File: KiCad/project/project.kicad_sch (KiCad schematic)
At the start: 8 parts, among them U1 NUCLEO-L476RG

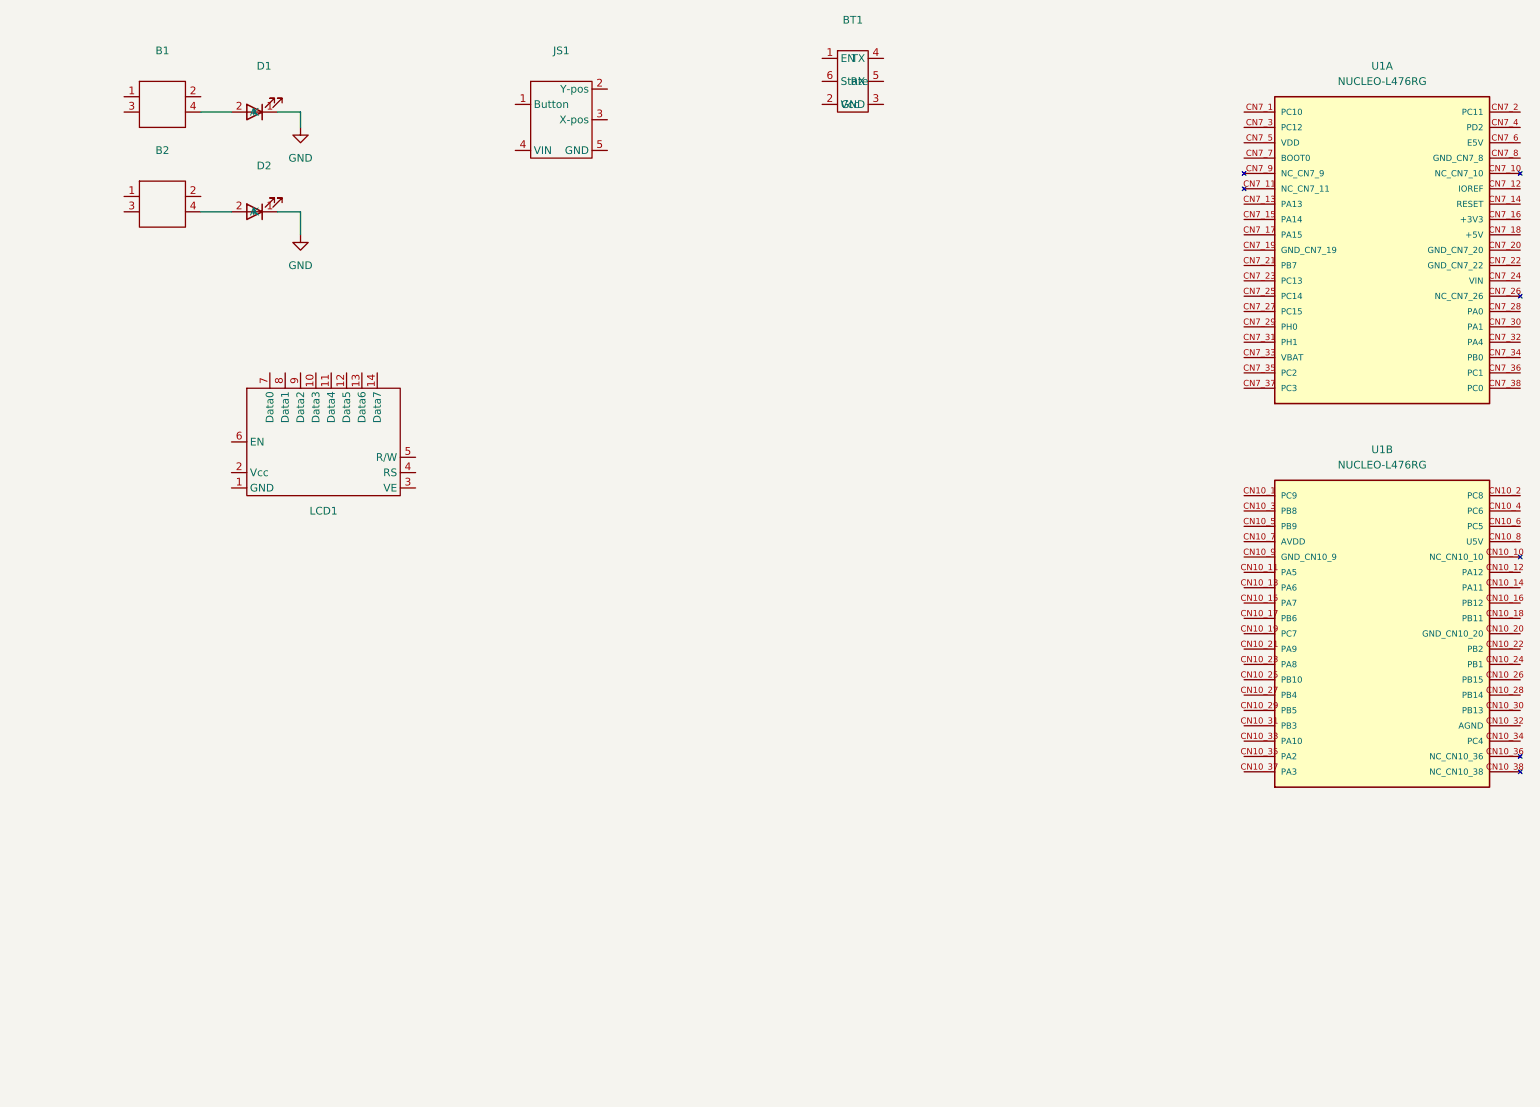
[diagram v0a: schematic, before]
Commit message: Updated PCB schematic and pinout for the ioc file because it was funky
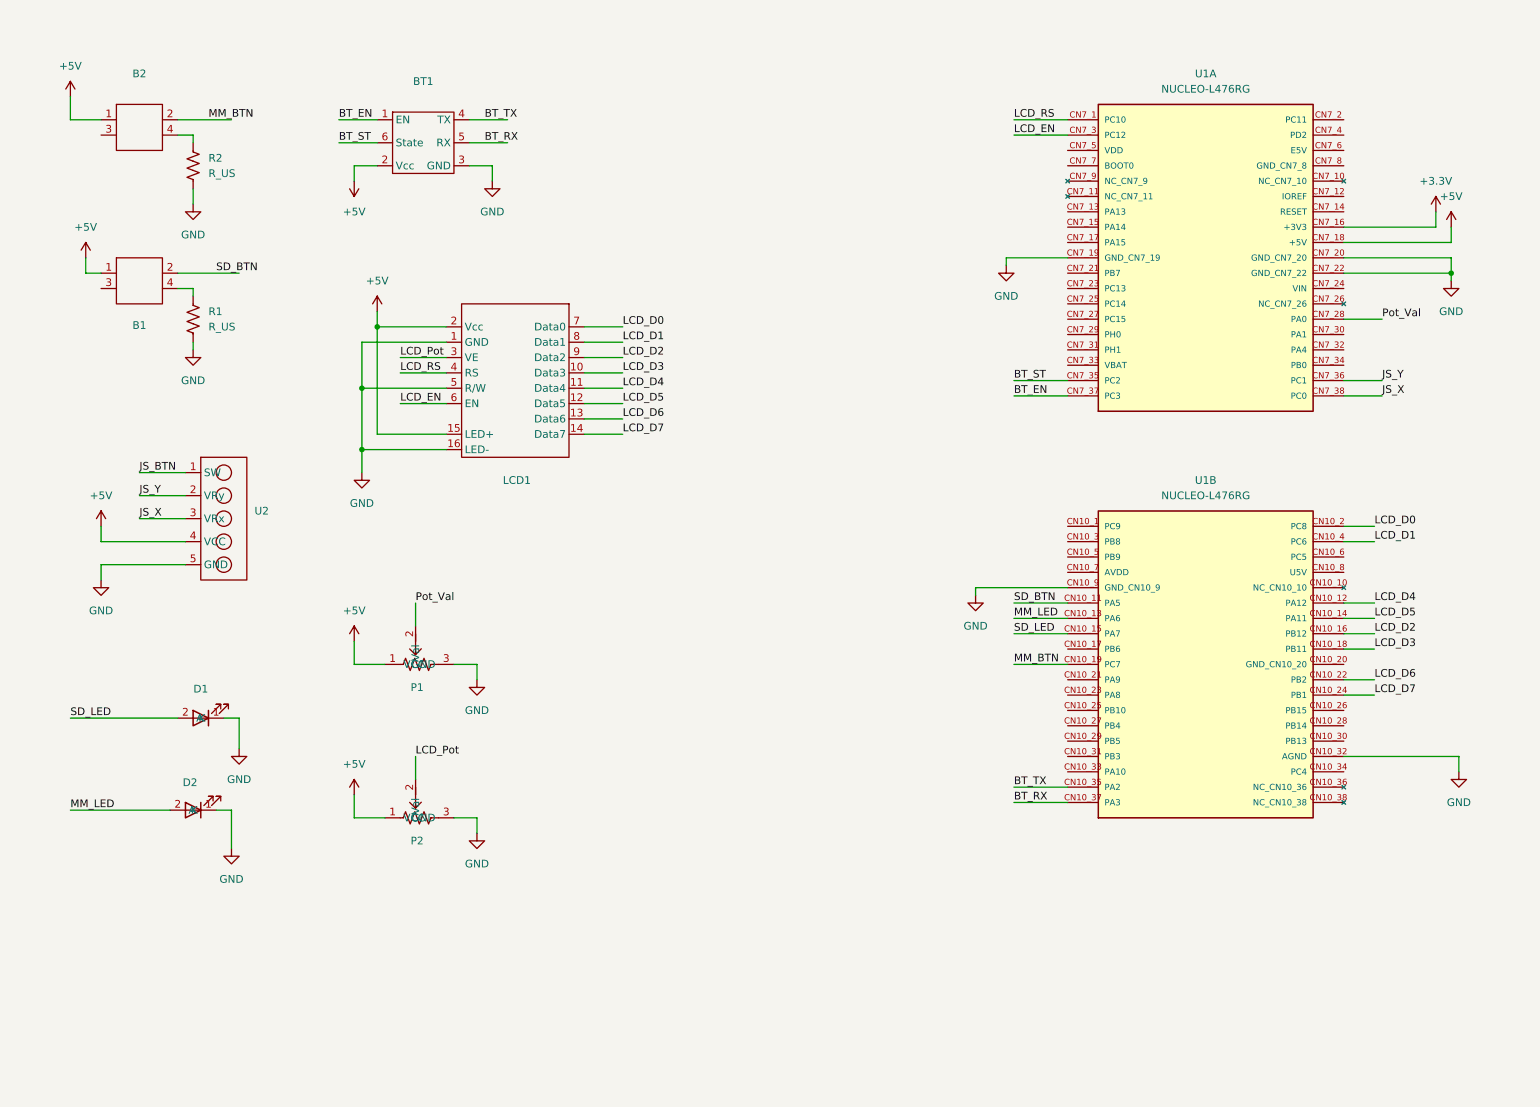
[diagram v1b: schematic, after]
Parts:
- removed JS1: ~, Embedded_Footprints:Joystick, symbol New_Library:JoyStick
- added P1, P2: ~, Embedded_Footprints:Potentiometer, symbol New_Library:Potentiometer
- added R1, R2: R_US, symbol Device:R_US
- added U2: ~, Embedded_Footprints:Joystick_Pins, symbol New_Library:Joystick_Header
- D1, D2: footprint Embedded_Footprints:LED -> Embedded_Footprints:LED_THRU
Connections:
- net GND: now also BT1.3 (GND), LCD1.1 (GND), LCD1.16 (LED-), LCD1.5 (R/W), U1.CN10_32 (AGND), U1.CN10_9 (GND_CN10_9), U1.CN7_19 (GND_CN7_19), U1.CN7_20 (GND_CN7_20), U1.CN7_22 (GND_CN7_22), P1.3 (GND), P2.3 (GND), R1.2, R2.2, U2.5 (GND)
- net BT_EN: now reaches BT1.1 (EN)
- net BT_EN: now also U1.CN7_37 (PC3)
- net +5V: now reaches BT1.2 (Vcc)
- net +5V: now also B1.1, B2.1, LCD1.15 (LED+), LCD1.2 (Vcc), U1.CN7_18 (+5V), P1.1 (VCC), P2.1 (VCC), U2.4 (VCC)
- net BT_TX: now reaches BT1.4 (TX)
- net BT_TX: now also U1.CN10_35 (PA2)
- net BT_RX: now reaches BT1.5 (RX)
- net BT_RX: now also U1.CN10_37 (PA3)
- net BT_ST: now reaches BT1.6 (State)
- net BT_ST: now also U1.CN7_35 (PC2)
- net SD_BTN: now reaches B1.2
- net SD_BTN: now also U1.CN10_11 (PA5)
- net at B1.4: now also R1.1; no longer D1.2 (A)
- net LCD_RS: now reaches U1.CN7_1 (PC10)
- net LCD_RS: now also LCD1.4 (RS)
- net +3.3V: now reaches U1.CN7_16 (+3V3)
- net Pot_Val: now reaches U1.CN7_28 (PA0)
- net Pot_Val: now also P1.2 (Val)
- net LCD_EN: now reaches U1.CN7_3 (PC12)
- net LCD_EN: now also LCD1.6 (EN)
- net JS_Y: now reaches U1.CN7_36 (PC1)
- net JS_Y: now also U2.2 (VRy)
- net JS_X: now reaches U1.CN7_38 (PC0)
- net JS_X: now also U2.3 (VRx)
- net at B2.4: now also R2.1; no longer D2.2 (A)
- net MM_BTN: now reaches B2.2
- net MM_BTN: now also U1.CN10_19 (PC7)
- net LCD_D4: now reaches U1.CN10_12 (PA12)
- net LCD_D4: now also LCD1.11 (Data4)
- net MM_LED: now reaches U1.CN10_13 (PA6)
- net MM_LED: now also D2.2 (A)
- net LCD_D5: now reaches U1.CN10_14 (PA11)
- net LCD_D5: now also LCD1.12 (Data5)
- net SD_LED: now reaches U1.CN10_15 (PA7)
- net SD_LED: now also D1.2 (A)
- net LCD_D2: now reaches U1.CN10_16 (PB12)
- net LCD_D2: now also LCD1.9 (Data2)
- net LCD_D3: now reaches U1.CN10_18 (PB11)
- net LCD_D3: now also LCD1.10 (Data3)
- net LCD_D0: now reaches U1.CN10_2 (PC8)
- net LCD_D0: now also LCD1.7 (Data0)
- net LCD_D6: now reaches U1.CN10_22 (PB2)
- net LCD_D6: now also LCD1.13 (Data6)
- net LCD_D7: now reaches U1.CN10_24 (PB1)
- net LCD_D7: now also LCD1.14 (Data7)
- net LCD_D1: now reaches U1.CN10_4 (PC6)
- net LCD_D1: now also LCD1.8 (Data1)
- net LCD_Pot: now reaches LCD1.3 (VE)
- net LCD_Pot: now also P2.2 (Val)
- new net JS_BTN: U2.1 (SW)
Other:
- moved on the sheet: B1, B2, BT1, D1, D2, U1A, U1B

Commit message: Update stuff :)
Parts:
- added H1: ~, Embedded_Footprints:OLED, symbol New_Library:OLED_Header
- R1, R2: footprint (none) -> Embedded_Footprints:RESC3216X65
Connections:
- net +3.3V: now also H1.2 (VCC)
- net BT_EN: now also U1.CN10_5 (PB9); no longer U1.CN7_37 (PC3)
- net BT_RX: now also U1.CN7_4 (PD2); no longer U1.CN10_37 (PA3)
- net BT_ST: now also U1.CN10_3 (PB8); no longer U1.CN7_35 (PC2)
- net BT_TX: now also U1.CN7_3 (PC12); no longer U1.CN10_35 (PA2)
- net GND: now also H1.1 (GND); no longer U1.CN10_32 (AGND)
- net LCD_D0: now also U1.CN10_22 (PB2); no longer U1.CN10_2 (PC8)
- net LCD_D1: now also U1.CN10_18 (PB11); no longer U1.CN10_4 (PC6)
- net LCD_D3: now also U1.CN10_14 (PA11); no longer U1.CN10_18 (PB11)
- net LCD_D5: now also U1.CN10_6 (PC5); no longer U1.CN10_14 (PA11)
- net LCD_D6: now also U1.CN10_4 (PC6); no longer U1.CN10_22 (PB2)
- net LCD_D7: now also U1.CN10_2 (PC8); no longer U1.CN10_24 (PB1)
- net LCD_EN: now also U1.CN10_24 (PB1); no longer U1.CN7_3 (PC12)
- net LCD_RS: now also U1.CN10_26 (PB15); no longer U1.CN7_1 (PC10)
- net SD_BTN: now also U1.CN10_17 (PB6); no longer U1.CN10_11 (PA5)
- net OLED_SDA: now reaches U1.CN10_28 (PB14)
- net OLED_SDA: now also H1.4 (SDA)
- net OLED_SCL: now reaches U1.CN10_30 (PB13)
- net OLED_SCL: now also H1.3 (SCL)
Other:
- moved on the sheet: D1, D2

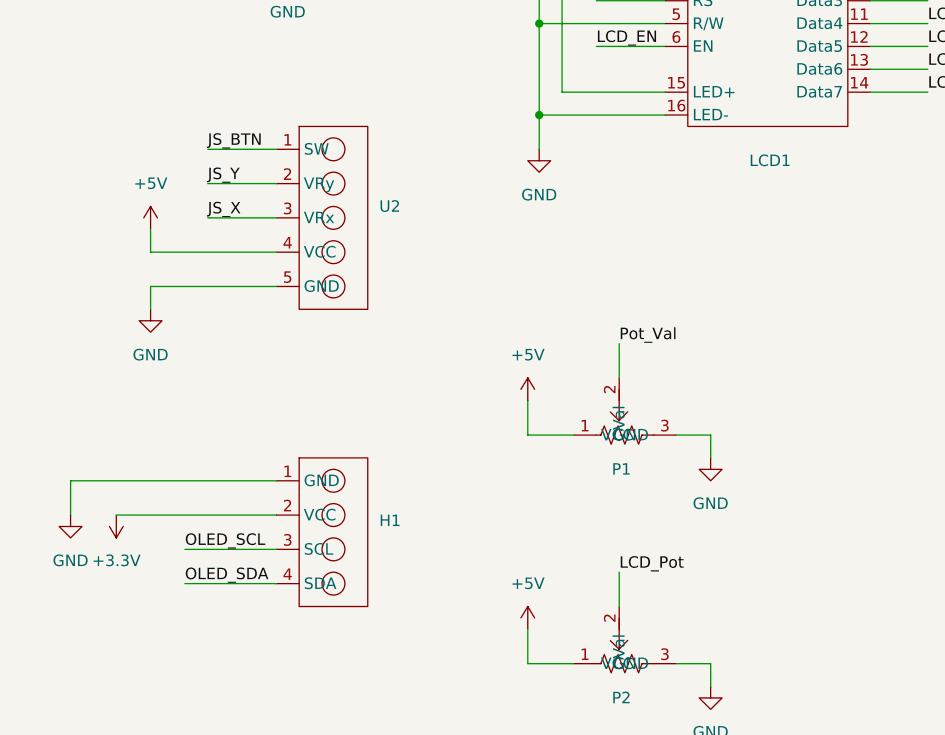
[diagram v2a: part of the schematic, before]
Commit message: Updated PCB for parallel capacitors
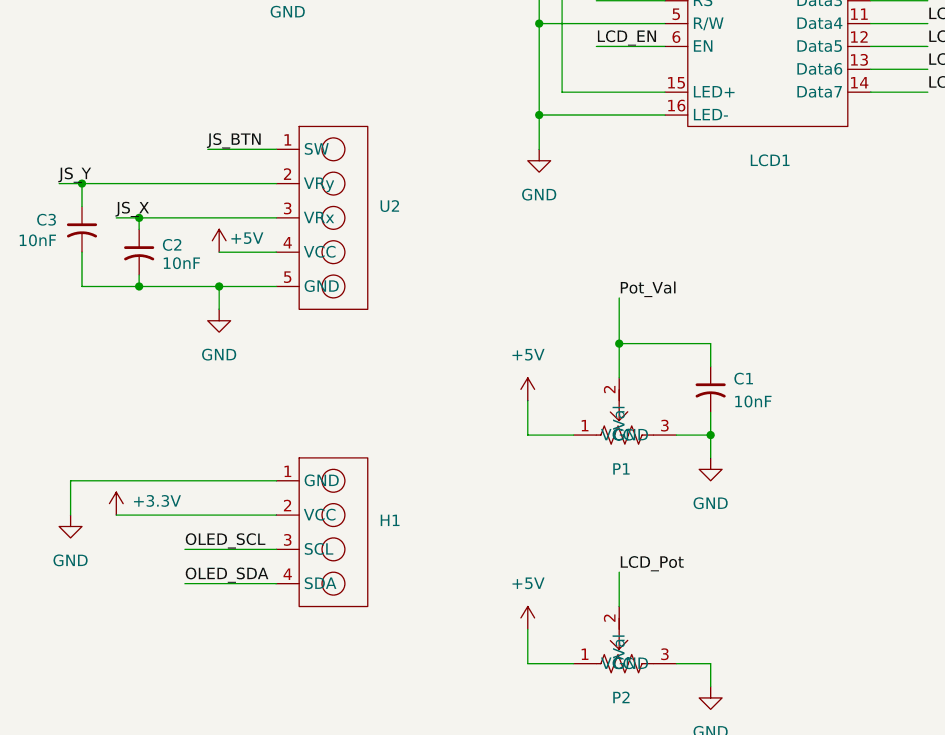
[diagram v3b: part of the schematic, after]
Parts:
- added C1, C2, C3: 10nF, Embedded_Footprints:CAPC340180_88N_KEM, symbol Device:C_Small_US
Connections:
- net GND: now also C1.2, C2.2, C3.2
- net JS_X: now also C2.1
- net JS_Y: now also C3.1
- net Pot_Val: now also C1.1
